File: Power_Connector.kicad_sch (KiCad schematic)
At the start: 3 parts, among them J4 AMASS XT60 Male, J5 AMASS XT60 Female

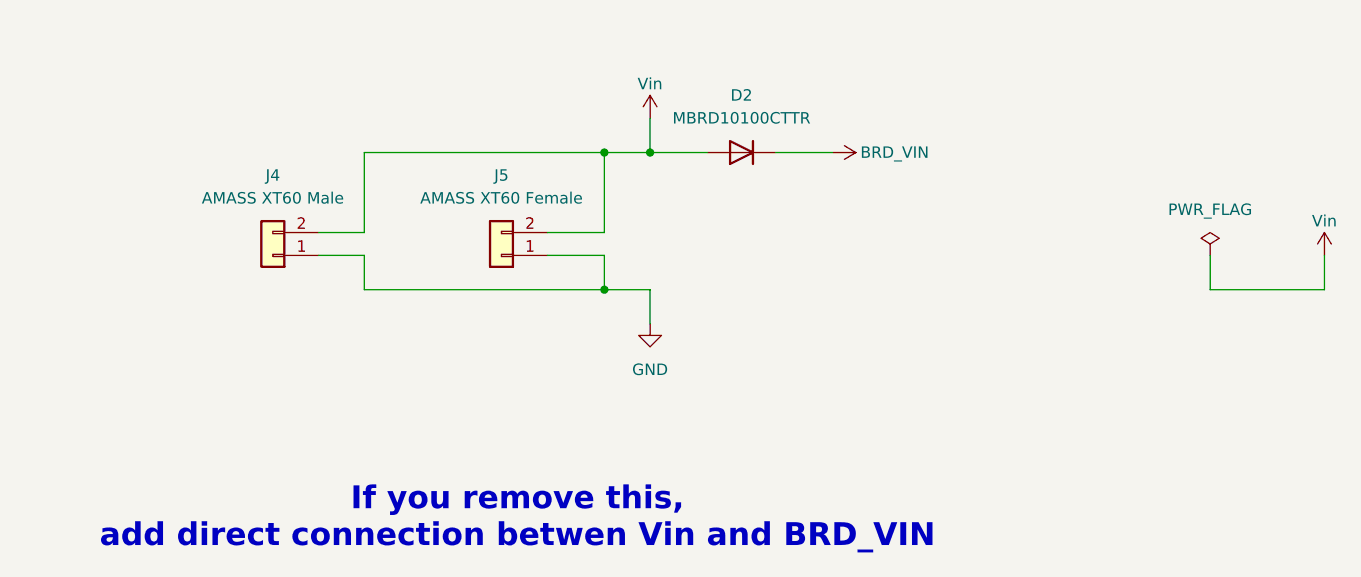
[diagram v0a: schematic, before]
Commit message: Added mechanical standard and updated readme
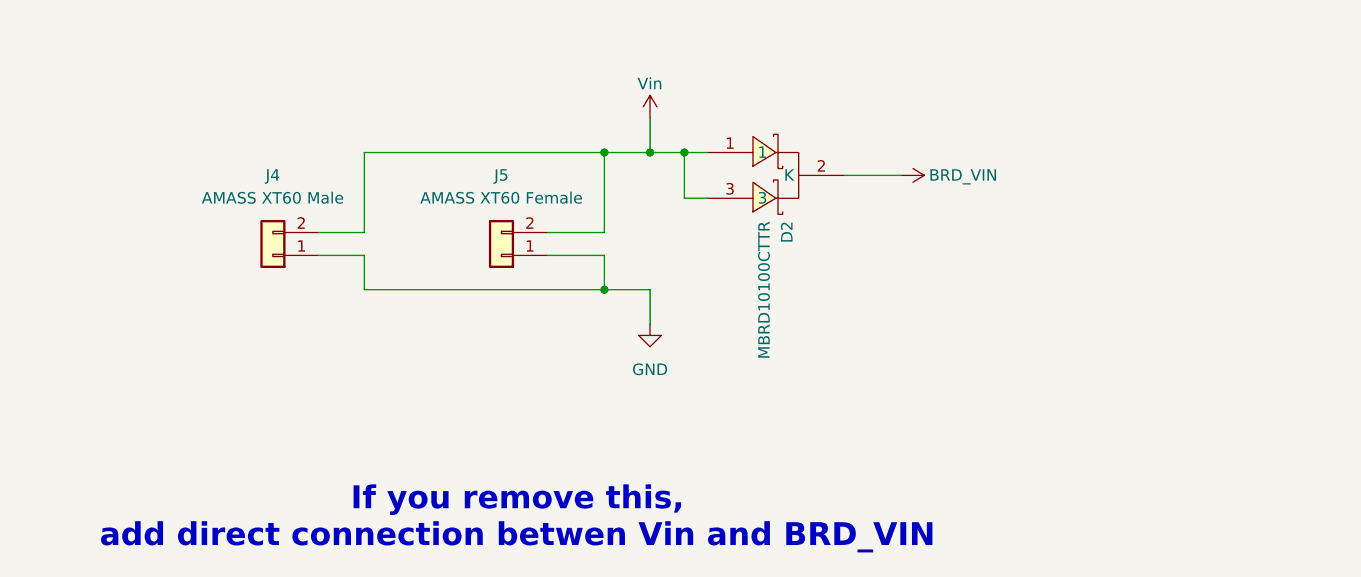
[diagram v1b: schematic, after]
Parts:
- removed D2: MBRD10100CTTR, symbol Device:D
- added D2: MBRD10100CTTR, SMC_MBRD10100CTTR:TO-252-3_L6.5-W5.8-P4.58-TL, symbol SMC_MBRD10100CTTR:MBRD10100CTTR
- J4, J5: now left out of the parts list
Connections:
- net BRD_VIN: now also D2.2 (K)
- net Vin: now also D2.1, D2.3

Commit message: updated XT60 place. added routing
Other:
- title: (none) -> MMS3 Stepper Controler
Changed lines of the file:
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@@
 	(generator_version "9.0")
 	(paper "A4")
+	(title_block
+		(title "MMS3 Stepper Controler")
+		(date "2026-02-25")
+		(rev "R0")
+		(comment 1 "Made by Wojciech Szafrański")
+		(comment 2 "Designed in poland")
+		(comment 3 "MMS3 Hat based on Chainbus")
+	)
 	(text "If you remove this, \nadd direct connection betwen Vin and BRD_VIN"
 		(exclude_from_sim no)

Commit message: moved I2C header to the side
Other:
- title: MMS3 Stepper Controler -> MMS3 Hat template small (Change Me)
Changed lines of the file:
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@@
 	(paper "A4")
 	(title_block
-		(title "MMS3 Stepper Controler")
+		(title "MMS3 Hat template small (Change Me)")
 		(date "2026-02-25")
-		(rev "R0")
+		(rev "A")
 		(comment 1 "Made by Wojciech Szafrański")
 		(comment 2 "Designed in poland")
-		(comment 3 "MMS3 Hat based on Chainbus")
 	)
 	(text "If you remove this, \nadd direct connection betwen Vin and BRD_VIN"

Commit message: Updated footprints
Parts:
- removed D2: MBRD10100CTTR, SMC_MBRD10100CTTR:TO-252-3_L6.5-W5.8-P4.58-TL, symbol SMC_MBRD10100CTTR:MBRD10100CTTR
- added D4: SS510C, SS510C:SMC_L7.1-W6.2-LS8.1-RD, symbol SS510C:SS510C
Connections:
- net BRD_VIN: now also D4.1 (K)
- net Vin: now also D4.2 (A)

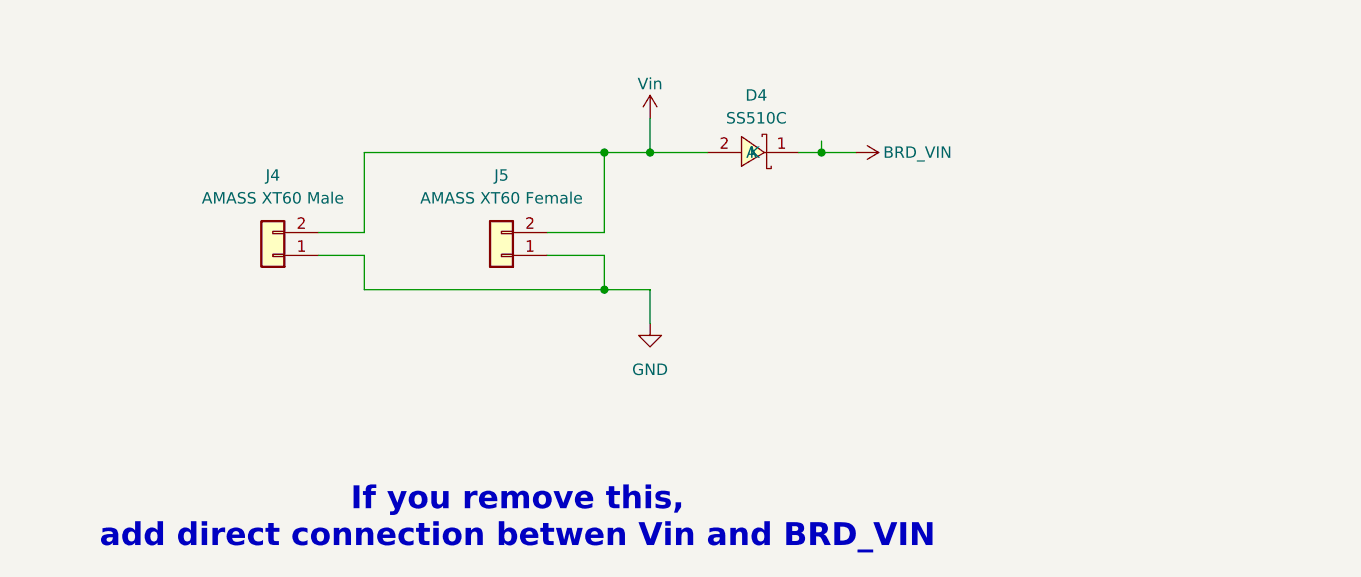
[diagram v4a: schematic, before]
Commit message: changed vin connector to hierarchical labels
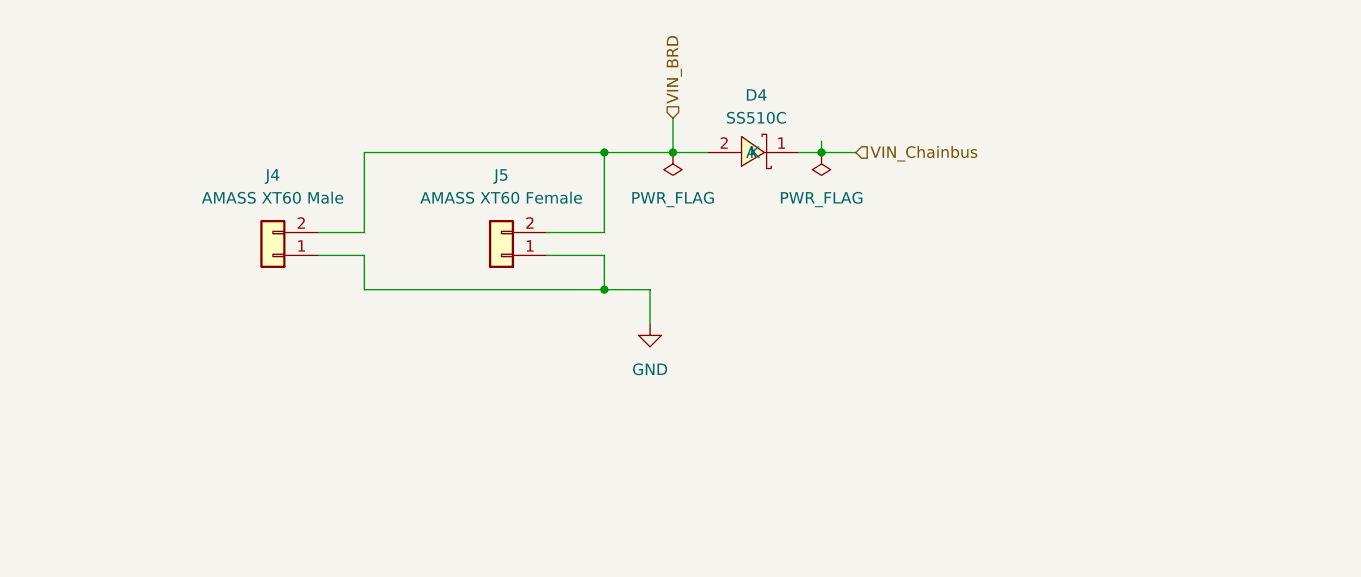
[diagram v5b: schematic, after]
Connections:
- net BRD_VIN renamed VIN_Chainbus
- net Vin renamed VIN_BRD
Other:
- note removed: "If you remove this, add direct connection betwen Vin and BRD_VIN"
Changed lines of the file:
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@@
 		(comment 2 "Designed in poland")
-	)
-	(text "If you remove this, \nadd direct connection betwen Vin and BRD_VIN"
-		(exclude_from_sim no)
-		(at 142.748 127 0)
-		(effects
-			(font
-				(size 2.54 2.54)
-				(thickness 0.508)
-				(bold yes)
-				(color 255 10 0 1)
-			)
-		)
 	)
 	(junction
@@
 	)
 	(junction
+		(at 160.02 86.36)
+		(diameter 0)
+		(color 0 0 0 0)
+	)
+	(junction
 		(at 176.53 86.36)
 		(diameter 0)
 		(color 0 0 0 0)
 	)
-	(junction
-		(at 157.48 86.36)
-		(diameter 0)
-		(color 0 0 0 0)
-	)
 	(wire
 		(pts
@@
 	(wire
 		(pts
-			(xy 157.48 86.36) (xy 163.83 86.36)
-		)
-		(stroke
-			(width 0)
-			(type default)
-		)
-	)
-	(wire
-		(pts
-			(xy 152.4 86.36) (xy 157.48 86.36)
+			(xy 152.4 86.36) (xy 160.02 86.36)
 		)
 		(stroke
@@
 	(wire
 		(pts
-			(xy 157.48 82.55) (xy 157.48 86.36)
+			(xy 160.02 82.55) (xy 160.02 86.36)
 		)
 		(stroke
@@
 	(wire
 		(pts
+			(xy 160.02 86.36) (xy 163.83 86.36)
+		)
+		(stroke
+			(width 0)
+			(type default)
+		)
+	)
+	(wire
+		(pts
 			(xy 173.99 86.36) (xy 176.53 86.36)
 		)
@@
 			(width 0)
 			(type default)
+		)
+	)
+	(hierarchical_label "VIN_BRD"
+		(shape input)
+		(at 160.02 82.55 90)
+		(effects
+			(font
+				(size 1.27 1.27)
+			)
+			(justify left)
+		)
+	)
+	(hierarchical_label "VIN_Chainbus"
+		(shape input)
+		(at 180.34 86.36 0)
+		(effects
+			(font
+				(size 1.27 1.27)
+			)
+			(justify left)
 		)
 	)
@@
 	)
 	(symbol
-		(lib_id "power:VCC")
-		(at 180.34 86.36 270)
-		(unit 1)
-		(body_style 1)
-		(exclude_from_sim no)
-		(in_bom yes)
-		(on_board yes)
-		(in_pos_files yes)
-		(dnp no)
-		(property "Reference" "#PWR041"
-			(at 176.53 86.36 0)
-			(hide yes)
-			(show_name no)
-			(do_not_autoplace no)
-			(effects
-				(font
-					(size 1.27 1.27)
-				)
-			)
-		)
-		(property "Value" "BRD_VIN"
-			(at 187.198 86.36 90)
-			(show_name no)
-			(do_not_autoplace no)
-			(effects
-				(font
-					(size 1.27 1.27)
-				)
-			)
-		)
-		(property "Footprint" ""
-			(at 180.34 86.36 0)
-			(hide yes)
-			(show_name no)
-			(do_not_autoplace no)
-			(effects
-				(font
-					(size 1.27 1.27)
-				)
-			)
-		)
-		(property "Datasheet" ""
-			(at 180.34 86.36 0)
-			(hide yes)
-			(show_name no)
-			(do_not_autoplace no)
-			(effects
-				(font
-					(size 1.27 1.27)
-				)
-			)
-		)
-		(property "Description" "Power symbol creates a global label with name \"VCC\""
-			(at 180.34 86.36 0)
-			(hide yes)
-			(show_name no)
-			(do_not_autoplace no)
-			(effects
-				(font
-					(size 1.27 1.27)
-				)
-			)
-		)
-		(pin "1"
-		)
-		(instances
-			(project "MMS3_hat_templates"
-				(path "/6596548a-44e0-46d8-8624-fd71cf4a3e17/f11c3b61-ae6a-4858-9d37-bbf426f44fb0"
-					(reference "#PWR041")
-					(unit 1)
-				)
-			)
-		)
-	)
-	(symbol
 		(lib_id "Connector_Generic:Conn_01x02")
 		(at 140.97 97.79 180)
@@
 	)
 	(symbol
-		(lib_id "power:VCC")
-		(at 157.48 82.55 0)
+		(lib_id "power:PWR_FLAG")
+		(at 176.53 86.36 180)
 		(unit 1)
 		(body_style 1)
@@
 		(in_pos_files yes)
 		(dnp no)
-		(property "Reference" "#PWR039"
-			(at 157.48 86.36 0)
-			(hide yes)
-			(show_name no)
-			(do_not_autoplace no)
-			(effects
-				(font
-					(size 1.27 1.27)
-				)
-			)
-		)
-		(property "Value" "Vin"
-			(at 157.48 78.74 0)
+		(fields_autoplaced yes)
+		(property "Reference" "#FLG02"
+			(at 176.53 88.265 0)
+			(hide yes)
+			(show_name no)
+			(do_not_autoplace no)
+			(effects
+				(font
+					(size 1.27 1.27)
+				)
+			)
+		)
+		(property "Value" "PWR_FLAG"
+			(at 176.53 91.44 0)
 			(show_name no)
 			(do_not_autoplace no)
@@
 		)
 		(property "Footprint" ""
-			(at 157.48 82.55 0)
+			(at 176.53 86.36 0)
 			(hide yes)
 			(show_name no)
@@
 		)
 		(property "Datasheet" ""
-			(at 157.48 82.55 0)
-			(hide yes)
-			(show_name no)
-			(do_not_autoplace no)
-			(effects
-				(font
-					(size 1.27 1.27)
-				)
-			)
-		)
-		(property "Description" "Power symbol creates a global label with name \"VCC\""
-			(at 157.48 82.55 0)
+			(at 176.53 86.36 0)
+			(hide yes)
+			(show_name no)
+			(do_not_autoplace no)
+			(effects
+				(font
+					(size 1.27 1.27)
+				)
+			)
+		)
+		(property "Description" "Special symbol for telling ERC where power comes from"
+			(at 176.53 86.36 0)
 			(hide yes)
 			(show_name no)
@@
 			(project "MMS3_hat_templates"
 				(path "/6596548a-44e0-46d8-8624-fd71cf4a3e17/f11c3b61-ae6a-4858-9d37-bbf426f44fb0"
-					(reference "#PWR039")
+					(reference "#FLG02")
 					(unit 1)
 				)
@@
 					(unit 1)
 				)
+			)
+		)
+	)
+	(symbol
+		(lib_id "power:PWR_FLAG")
+		(at 160.02 86.36 180)
+		(unit 1)
+		(body_style 1)
+		(exclude_from_sim no)
+		(in_bom yes)
+		(on_board yes)
+		(in_pos_files yes)
+		(dnp no)
+		(fields_autoplaced yes)
+		(property "Reference" "#FLG03"
+			(at 160.02 88.265 0)
+			(hide yes)
+			(show_name no)
+			(do_not_autoplace no)
+			(effects
+				(font
+					(size 1.27 1.27)
+				)
+			)
+		)
+		(property "Value" "PWR_FLAG"
+			(at 160.02 91.44 0)
+			(show_name no)
+			(do_not_autoplace no)
+			(effects
+				(font
+					(size 1.27 1.27)
+				)
+			)
+		)
+		(property "Footprint" ""
+			(at 160.02 86.36 0)
+			(hide yes)
+			(show_name no)
+			(do_not_autoplace no)
+			(effects
+				(font
+					(size 1.27 1.27)
+				)
+			)
+		)
+		(property "Datasheet" ""
+			(at 160.02 86.36 0)
+			(hide yes)
+			(show_name no)
+			(do_not_autoplace no)
+			(effects
+				(font
+					(size 1.27 1.27)
+				)
+			)
+		)
+		(property "Description" "Special symbol for telling ERC where power comes from"
+			(at 160.02 86.36 0)
+			(hide yes)
+			(show_name no)
+			(do_not_autoplace no)
+			(effects
+				(font
+					(size 1.27 1.27)
+				)
+			)
+		)
+		(pin "1"
+		)
+		(instances
+			(project "MMS3_hat_templates"
+				(path "/6596548a-44e0-46d8-8624-fd71cf4a3e17/f11c3b61-ae6a-4858-9d37-bbf426f44fb0"
+					(reference "#FLG03")
+					(unit 1)
+				)

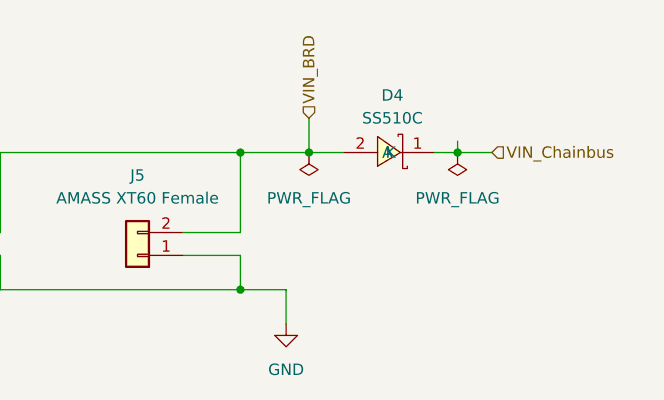
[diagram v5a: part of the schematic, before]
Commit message: changed VIN diode from 1.5A extended to 1A basic assembly
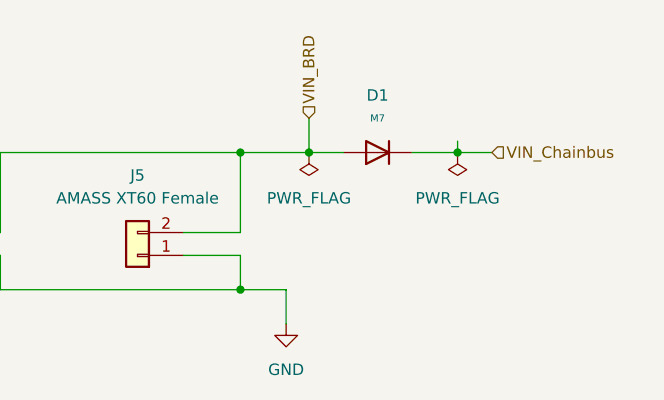
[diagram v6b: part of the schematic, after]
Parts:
- removed D4: SS510C, SS510C:SMC_L7.1-W6.2-LS8.1-RD, symbol SS510C:SS510C
- added D1: M7, PCM_JLCPCB:D_SMA, symbol PCM_JLCPCB-Diodes:General,M7
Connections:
- net VIN_BRD: now also D1.2
- net VIN_Chainbus: now also D1.1
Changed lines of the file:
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@@
 	(wire
 		(pts
-			(xy 173.99 86.36) (xy 176.53 86.36)
+			(xy 125.73 86.36) (xy 152.4 86.36)
 		)
 		(stroke
@@
 	(wire
 		(pts
-			(xy 125.73 86.36) (xy 152.4 86.36)
+			(xy 152.4 101.6) (xy 152.4 97.79)
 		)
 		(stroke
@@
 	(wire
 		(pts
-			(xy 152.4 101.6) (xy 152.4 97.79)
+			(xy 176.53 86.36) (xy 180.34 86.36)
 		)
 		(stroke
@@
 	(wire
 		(pts
-			(xy 176.53 86.36) (xy 180.34 86.36)
+			(xy 171.45 86.36) (xy 176.53 86.36)
 		)
 		(stroke
@@
 	)
 	(symbol
-		(lib_id "SS510C:SS510C")
-		(at 168.91 86.36 180)
+		(lib_id "PCM_JLCPCB-Diodes:General,M7")
+		(at 167.64 86.36 90)
 		(unit 1)
 		(body_style 1)
@@
 		(dnp no)
 		(fields_autoplaced yes)
-		(property "Reference" "D4"
-			(at 169.29 80.01 0)
-			(show_name no)
-			(do_not_autoplace no)
-			(effects
-				(font
-					(size 1.27 1.27)
-				)
-			)
-		)
-		(property "Value" "SS510C"
-			(at 169.29 82.55 0)
-			(show_name no)
-			(do_not_autoplace no)
-			(effects
-				(font
-					(size 1.27 1.27)
-				)
-			)
-		)
-		(property "Footprint" "SS510C:SMC_L7.1-W6.2-LS8.1-RD"
-			(at 168.91 78.74 0)
-			(hide yes)
-			(show_name no)
-			(do_not_autoplace no)
-			(effects
-				(font
-					(size 1.27 1.27)
-				)
-			)
-		)
-		(property "Datasheet" "https://lcsc.com/product-detail/Schottky-Barrier-Diodes-SBD_SS510C_C123944.html"
-			(at 168.91 76.2 0)
-			(hide yes)
-			(show_name no)
-			(do_not_autoplace no)
-			(effects
-				(font
-					(size 1.27 1.27)
-				)
-			)
-		)
-		(property "Description" ""
-			(at 168.91 86.36 0)
-			(hide yes)
-			(show_name no)
-			(do_not_autoplace no)
-			(effects
-				(font
-					(size 1.27 1.27)
-				)
-			)
-		)
-		(property "Manufacturer" "晶导微电子"
-			(at 168.91 73.66 0)
-			(hide yes)
-			(show_name no)
-			(do_not_autoplace no)
-			(effects
-				(font
-					(size 1.27 1.27)
-				)
-			)
-		)
-		(property "MPN" "SS510C"
-			(at 168.91 71.12 0)
-			(hide yes)
-			(show_name no)
-			(do_not_autoplace no)
-			(effects
-				(font
-					(size 1.27 1.27)
-				)
-			)
-		)
-		(property "LCSC Part" "C123944"
-			(at 168.91 68.58 0)
-			(hide yes)
-			(show_name no)
-			(do_not_autoplace no)
-			(effects
-				(font
-					(size 1.27 1.27)
-				)
-			)
+		(property "Reference" "D1"
+			(at 167.64 80.01 90)
+			(show_name no)
+			(do_not_autoplace no)
+			(effects
+				(font
+					(size 1.27 1.27)
+				)
+			)
+		)
+		(property "Value" "M7"
+			(at 167.64 82.55 90)
+			(show_name no)
+			(do_not_autoplace no)
+			(effects
+				(font
+					(size 0.8 0.8)
+				)
+			)
+		)
+		(property "Footprint" "PCM_JLCPCB:D_SMA"
+			(at 167.64 88.138 90)
+			(hide yes)
+			(show_name no)
+			(do_not_autoplace no)
+			(effects
+				(font
+					(size 1.27 1.27)
+				)
+			)
+		)
+		(property "Datasheet" "https://www.lcsc.com/datasheet/lcsc_datasheet_2407101107_MDD-Microdiode-Semiconductor-M7_C95872.pdf"
+			(at 167.64 86.36 0)
+			(hide yes)
+			(show_name no)
+			(do_not_autoplace no)
+			(effects
+				(font
+					(size 1.27 1.27)
+				)
+			)
+		)
+		(property "Description" "1A Independent Type 1kV 1.1V@1A SMA(DO-214AC) Diodes - General Purpose ROHS"
+			(at 167.64 86.36 0)
+			(hide yes)
+			(show_name no)
+			(do_not_autoplace no)
+			(effects
+				(font
+					(size 1.27 1.27)
+				)
+			)
+		)
+		(property "LCSC" "C95872"
+			(at 167.64 86.36 0)
+			(hide yes)
+			(show_name no)
+			(do_not_autoplace no)
+			(effects
+				(font
+					(size 1.27 1.27)
+				)
+			)
+		)
+		(property "Stock" "3256855"
+			(at 167.64 86.36 0)
+			(hide yes)
+			(show_name no)
+			(do_not_autoplace no)
+			(effects
+				(font
+					(size 1.27 1.27)
+				)
+			)
+		)
+		(property "Price" "0.011USD"
+			(at 167.64 86.36 0)
+			(hide yes)
+			(show_name no)
+			(do_not_autoplace no)
+			(effects
+				(font
+					(size 1.27 1.27)
+				)
+			)
+		)
+		(property "Process" "SMT"
+			(at 167.64 86.36 0)
+			(hide yes)
+			(show_name no)
+			(do_not_autoplace no)
+			(effects
+				(font
+					(size 1.27 1.27)
+				)
+			)
+		)
+		(property "Minimum Qty" "5"
+			(at 167.64 86.36 0)
+			(hide yes)
+			(show_name no)
+			(do_not_autoplace no)
+			(effects
+				(font
+					(size 1.27 1.27)
+				)
+			)
+		)
+		(property "Attrition Qty" "10"
+			(at 167.64 86.36 0)
+			(hide yes)
+			(show_name no)
+			(do_not_autoplace no)
+			(effects
+				(font
+					(size 1.27 1.27)
+				)
+			)
+		)
+		(property "Class" "Basic Component"
+			(at 167.64 86.36 0)
+			(hide yes)
+			(show_name no)
+			(do_not_autoplace no)
+			(effects
+				(font
+					(size 1.27 1.27)
+				)
+			)
+		)
+		(property "Category" "Diodes,Diodes - General Purpose"
+			(at 167.64 86.36 0)
+			(hide yes)
+			(show_name no)
+			(do_not_autoplace no)
+			(effects
+				(font
+					(size 1.27 1.27)
+				)
+			)
+		)
+		(property "Manufacturer" "MDD（Microdiode Electronics）"
+			(at 167.64 86.36 0)
+			(hide yes)
+			(show_name no)
+			(do_not_autoplace no)
+			(effects
+				(font
+					(size 1.27 1.27)
+				)
+			)
+		)
+		(property "Part" "M7"
+			(at 167.64 86.36 0)
+			(hide yes)
+			(show_name no)
+			(do_not_autoplace no)
+			(effects
+				(font
+					(size 1.27 1.27)
+				)
+			)
+		)
+		(property "Rectified Current" "1A"
+			(at 167.64 86.36 0)
+			(hide yes)
+			(show_name no)
+			(do_not_autoplace no)
+			(effects
+				(font
+					(size 1.27 1.27)
+				)
+			)
+		)
+		(property "Forward Voltage (Vf@If)" "1.1V@1A"
+			(at 167.64 86.36 0)
+			(hide yes)
+			(show_name no)
+			(do_not_autoplace no)
+			(effects
+				(font
+					(size 1.27 1.27)
+				)
+			)
+		)
+		(property "Reverse Voltage (Vr)" "1kV"
+			(at 167.64 86.36 0)
+			(hide yes)
+			(show_name no)
+			(do_not_autoplace no)
+			(effects
+				(font
+					(size 1.27 1.27)
+				)
+			)
+		)
+		(property "Diode Configuration" "Independent Type"
+			(at 167.64 86.36 0)
+			(hide yes)
+			(show_name no)
+			(do_not_autoplace no)
+			(effects
+				(font
+					(size 1.27 1.27)
+				)
+			)
+		)
+		(property "Reverse Leakage Current" "5uA@1kV"
+			(at 167.64 86.36 0)
+			(hide yes)
+			(show_name no)
+			(do_not_autoplace no)
+			(effects
+				(font
+					(size 1.27 1.27)
+				)
+			)
+		)
+		(pin "1"
 		)
 		(pin "2"
-		)
-		(pin "1"
 		)
 		(instances
 			(project "MMS3_hat_templates"
 				(path "/6596548a-44e0-46d8-8624-fd71cf4a3e17/f11c3b61-ae6a-4858-9d37-bbf426f44fb0"
-					(reference "D4")
+					(reference "D1")
 					(unit 1)
 				)
